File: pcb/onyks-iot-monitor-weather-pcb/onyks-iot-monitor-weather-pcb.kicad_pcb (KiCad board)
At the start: 2 copper layers, 100 x 100 mm, 25 parts, among them J1 53398-0371, J10 Conn_01x02_Pin, J2 53398-0371, J3 53048-0810, J4 53398-0371, J5 53398-0371, J6 53398-0371, J7 53398-0371, J8 53398-0371, J9 53398-0371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

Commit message: Updated schematic, changed and added couple of elements: 1.Changed buttons; 2.Changed Voltage Regulator; 3.Changed LED; 4.Added JTAG interface; 5.Added UART for programming; 6.Added other elements like capacitors etc.
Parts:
- S1: value BOOT -> PTS636_SK25F_SMTR_LFS; footprint 1bmoje:18259106 -> 1bmoje:PTS636SK25FSMTRLFS
- S2: value ENABLE -> PTS636_SK25F_SMTR_LFS; footprint 1bmoje:18259106 -> 1bmoje:PTS636SK25FSMTRLFS
- moved S2 33.9 mm to (199.2, 94.5)
- moved S1 20.0 mm to (199.2, 89.7)

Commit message: Done my version of PCB
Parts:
- removed U2: AMS1117, Package_TO_SOT_SMD:SOT-223-3_TabPin2
- added C6: 22uF, Capacitor_SMD:C_0201_0603Metric, F.Cu at (94.7, 54.8)
- added C7: 22uF, Capacitor_SMD:C_0201_0603Metric, F.Cu at (91.9, 54.8)
- added C8: 22uF, Capacitor_SMD:C_0201_0603Metric, F.Cu at (133.9, 78.5)
- added D1: WS2812B, LED_SMD:LED_WS2812B_PLCC4_5.0x5.0mm_P3.2mm, F.Cu at (154.1, 51.6)
- added J11: Conn_01x06_Pin, Connector_PinHeader_2.54mm:PinHeader_1x06_P2.54mm_Vertical, F.Cu at (169.0, 69.0)
- added J12: Conn_02x05_Odd_Even, Connector_PinHeader_2.54mm:PinHeader_2x05_P2.54mm_Vertical, F.Cu at (119.5, 86.5)
- added J13: Conn_01x02_Pin, Connector_PinHeader_2.54mm:PinHeader_1x02_P2.54mm_Vertical, F.Cu at (87.2, 57.8)
- added U3: TLV75733PDBV, Package_TO_SOT_SMD:SOT-23-5, F.Cu at (93.9, 60.3)
- J10: footprint Connector_Molex:Molex_SL_171971-0002_1x02_P2.54mm_Vertical -> Connector_PinHeader_2.54mm:PinHeader_1x02_P2.54mm_Vertical
- moved C4 51.8 mm to (164.5, 73.6), turned to 90 degrees
- moved J3 40.4 mm to (144.8, 83.5), turned to 180 degrees
- moved J1 40.2 mm to (101.7, 66.4)
- moved C5 39.0 mm to (173.7, 88.0), turned to 0 degrees
- moved J9 36.0 mm to (156.7, 72.9)
- moved J10 34.4 mm to (87.0, 69.0), turned to 0 degrees
- moved J7 32.3 mm to (101.7, 60.9)
- moved J2 31.6 mm to (101.7, 55.4)
- moved J6 31.4 mm to (101.7, 86.4)
- moved J4 31.4 mm to (101.7, 73.4)
- moved J5 31.4 mm to (101.7, 79.9)
- moved C2 30.3 mm to (118.0, 50.1), turned to 90 degrees
- moved S1 29.7 mm to (172.7, 76.2)
- moved S2 28.9 mm to (172.7, 83.0)
- moved Q1 28.2 mm to (88.4, 75.7)
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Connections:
- U1 pad 13: /Hall 6 -> /MTMS
- U1 pad 14: /DHT22 -> /MTDI
- U1 pad 16: /SEN0219 -> /MTCK
- U1 pad 23: /PMS_SELECT -> /MTDO
- U1 pad 26: unconnected-(U1-IO4-Pad26) -> /DHT22
- U1 pad 27: unconnected-(U1-IO16-Pad27) -> /UART_PROGRAM_RXD
- U1 pad 28: unconnected-(U1-IO17-Pad28) -> /UART_PROGRAM_TXD
- U1 pad 29: unconnected-(U1-IO5-Pad29) -> /SEN0219
- U1 pad 30: unconnected-(U1-IO18-Pad30) -> /UART_PROGRAM_DTR
- U1 pad 31: unconnected-(U1-IO19-Pad31) -> /UART_PROGRAM_RTS
- U1 pad 33: unconnected-(U1-IO21-Pad33) -> /PMS_SELECT
- U1 pad 37: unconnected-(U1-IO23-Pad37) -> /LED
- U1 pad 9: unconnected-(U1-IO33-Pad9) -> /Hall 6
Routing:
- net GND: track 256.8 -> 100.2 mm, vias 7 -> 17
- net /3V3: track 118.6 -> 213.6 mm, vias 6 -> 8
- net /EN: track 103.2 -> 190.7 mm, vias 2 -> 5
- net VCC: track 138.5 -> 223.2 mm, vias 9 -> 11
- net /MTMS: track 0.00 -> 33.2 mm
- net /IO0: track 137.0 -> 104.7 mm, vias 0 -> 4
- net /DHT22: track 50.8 -> 20.8 mm
- net /UART_PROGRAM_DTR: track 0.00 -> 28.4 mm
- net /UART_PROGRAM_RTS: track 0.00 -> 27.9 mm
- net /MTDO: track 0.00 -> 27.3 mm, vias 0 -> 5
- net /UART_PROGRAM_RXD: track 0.00 -> 27.3 mm, vias 0 -> 1
- net /UART_PROGRAM_TXD: track 0.00 -> 27.2 mm, vias 0 -> 1
- net /MTDI: track 0.00 -> 23.6 mm
- net /MTCK: track 0.00 -> 22.0 mm, vias 0 -> 2
- net /PMS_PWM: track 40.8 -> 58.4 mm, vias 1 -> 5
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- added copper zone on B.Cu, net GND
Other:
- board size 100 x 100 mm -> 100 x 55.8 mm

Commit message: Few corrections, small ammount of parts were not connected to the ground.
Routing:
- net GND: track 100.2 -> 118.6 mm, vias 17 -> 20
- net /3V3: track 213.6 -> 226.6 mm, vias 8 -> 10
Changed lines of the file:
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@@
+	)
+	(segment
+		(start 96.25 54.5)
+		(end 96 54.75)
+		(width 0.4)
+		(layer "F.Cu")
+		(net 1)
 	)
 	(segment
@@
 	)
 	(segment
+		(start 173.36 88)
+		(end 171.75 88)
+		(width 0.4)
+		(layer "F.Cu")
+		(net 1)
+	)
+	(segment
+		(start 131.75 72.7)
+		(end 131.75 71)
+		(width 0.6)
+		(layer "F.Cu")
+		(net 1)
+	)
+	(segment
 		(start 149.5 50)
 		(end 147.5 50)
@@
 	)
 	(segment
+		(start 92.225 54.75)
+		(end 92.225 53.025)
+		(width 0.4)
+		(layer "F.Cu")
+		(net 1)
+	)
+	(segment
+		(start 131.8 78.5)
+		(end 132.5 78.5)
+		(width 0.6)
+		(layer "F.Cu")
+		(net 1)
+	)
+	(segment
 		(start 118 48.86)
 		(end 118 49.685)
@@
 	)
 	(segment
+		(start 133.675 75.325)
+		(end 132.5 76.5)
+		(width 0.4)
+		(layer "F.Cu")
+		(net 1)
+	)
+	(segment
 		(start 101.7 53.55)
 		(end 101.7 55.25)
@@
 	)
 	(segment
+		(start 133.675 74.3)
+		(end 133.675 75.325)
+		(width 0.4)
+		(layer "F.Cu")
+		(net 1)
+	)
+	(segment
+		(start 96.25 53)
+		(end 96.25 54.5)
+		(width 0.4)
+		(layer "F.Cu")
+		(net 1)
+	)
+	(segment
 		(start 122.25 89)
 		(end 122 88.75)
@@
 	)
 	(segment
-		(start 131.8 78.5)
-		(end 133.61 78.5)
-		(width 0.6)
+		(start 92.225 53.025)
+		(end 92.25 53)
+		(width 0.2)
+		(layer "F.Cu")
+		(net 1)
+	)
+	(segment
+		(start 96 54.75)
+		(end 95.05 54.75)
+		(width 0.4)
+		(layer "F.Cu")
+		(net 1)
+	)
+	(segment
+		(start 132.5 76.5)
+		(end 132.5 78.5)
+		(width 0.4)
 		(layer "F.Cu")
 		(net 1)
@@
 	)
 	(segment
+		(start 132.5 78.5)
+		(end 133.61 78.5)
+		(width 0.6)
+		(layer "F.Cu")
+		(net 1)
+	)
+	(segment
+		(start 131.5 70.75)
+		(end 127.75 70.75)
+		(width 0.6)
+		(layer "F.Cu")
+		(net 1)
+	)
+	(segment
+		(start 131.75 71)
+		(end 131.5 70.75)
+		(width 0.6)
+		(layer "F.Cu")
+		(net 1)
+	)
+	(segment
 		(start 115.15 48.85)
 		(end 115.16 48.86)
@@
 	)
 	(via
+		(at 92.25 53)
+		(size 1.2)
+		(drill 0.6)
+		(layers "F.Cu" "B.Cu")
+		(free yes)
+		(net 1)
+	)
+	(via
 		(at 101.7 59.2)
 		(size 1.2)
@@
 	)
 	(via
+		(at 171.75 88)
+		(size 1.2)
+		(drill 0.6)
+		(layers "F.Cu" "B.Cu")
+		(net 1)
+	)
+	(via
 		(at 160.25 72.75)
 		(size 1.2)
@@
 	)
 	(via
+		(at 96.25 53)
+		(size 1.2)
+		(drill 0.6)
+		(layers "F.Cu" "B.Cu")
+		(free yes)
+		(net 1)
+	)
+	(via
 		(at 122.75 54.25)
 		(size 1.2)
@@
 		(drill 0.6)
 		(layers "F.Cu" "B.Cu")
+		(net 1)
+	)
+	(segment
+		(start 146 83.5)
+		(end 146 81.75)
+		(width 0.6)
+		(layer "B.Cu")
 		(net 1)
 	)
@@
 	)
 	(segment
+		(start 132.45 74.3)
+		(end 133.025 74.3)
+		(width 0.4)
+		(layer "F.Cu")
+		(net 35)
+	)
+	(segment
 		(start 119.46 89.46)
 		(end 120 90)
 		(width 0.6)
+		(layer "F.Cu")
+		(net 35)
+	)
+	(segment
+		(start 131.75 75)
+		(end 132.45 74.3)
+		(width 0.4)
 		(layer "F.Cu")
 		(net 35)
@@
 	)
 	(segment
+		(start 133.7 71.2)
+		(end 133.7 72.7)
+		(width 0.4)
+		(layer "F.Cu")
+		(net 35)
+	)
+	(segment
 		(start 136.75 78.5)
 		(end 134.41 78.5)
@@
 		(net 35)
 	)
+	(segment
+		(start 131.25 75)
+		(end 131.75 75)
+		(width 0.4)
+		(layer "F.Cu")
+		(net 35)
+	)
 	(via
 		(at 95 57.25)
@@
 		(size 1.2)
 		(drill 0.6)
+		(layers "F.Cu" "B.Cu")
+		(net 35)
+	)
+	(via
+		(at 131.25 75)
+		(size 0.6)
+		(drill 0.3)
+		(layers "F.Cu" "B.Cu")
+		(net 35)
+	)
+	(via
+		(at 133.7 71.2)
+		(size 0.6)
+		(drill 0.3)
 		(layers "F.Cu" "B.Cu")
 		(net 35)
@@
 	)
 	(segment
+		(start 131.25 75)
+		(end 131.25 74)
+		(width 0.4)
+		(layer "B.Cu")
+		(net 35)
+	)
+	(segment
+		(start 131.5 73.75)
+		(end 134.325 73.75)
+		(width 0.4)
+		(layer "B.Cu")
+		(net 35)
+	)
+	(segment
 		(start 99.75 49.75)
 		(end 101.5 49.75)
@@
 		(end 116.75 51.75)
 		(width 0.6)
+		(layer "B.Cu")
+		(net 35)
+	)
+	(segment
+		(start 134.325 73.75)
+		(end 134.325 76.25)
+		(width 0.4)
 		(layer "B.Cu")
 		(net 35)
@@
 	)
 	(segment
+		(start 133.7 71.95)
+		(end 134.325 72.575)
+		(width 0.4)
+		(layer "B.Cu")
+		(net 35)
+	)
+	(segment
+		(start 133.7 71.2)
+		(end 133.7 71.95)
+		(width 0.4)
+		(layer "B.Cu")
+		(net 35)
+	)
+	(segment
 		(start 95 91.5)
 		(end 96 92.5)
@@
 	)
 	(segment
+		(start 131.25 74)
+		(end 131.5 73.75)
+		(width 0.4)
+		(layer "B.Cu")
+		(net 35)
+	)
+	(segment
 		(start 136.75 77.5)
 		(end 136.75 78.5)
@@
 		(layer "B.Cu")
 		(net 35)
+	)
+	(segment
+		(start 134.325 72.575)
+		(end 134.325 73.75)
+		(width 0.4)
+		(layer "B.Cu")
+		(net 35)

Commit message: Changed ground planes, and overall small changes
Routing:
- net /3V3: track 226.6 -> 230.1 mm
- net /PMS_PWM: track 58.4 -> 58.1 mm, vias 5 -> 4
- net GND: vias 20 -> 19

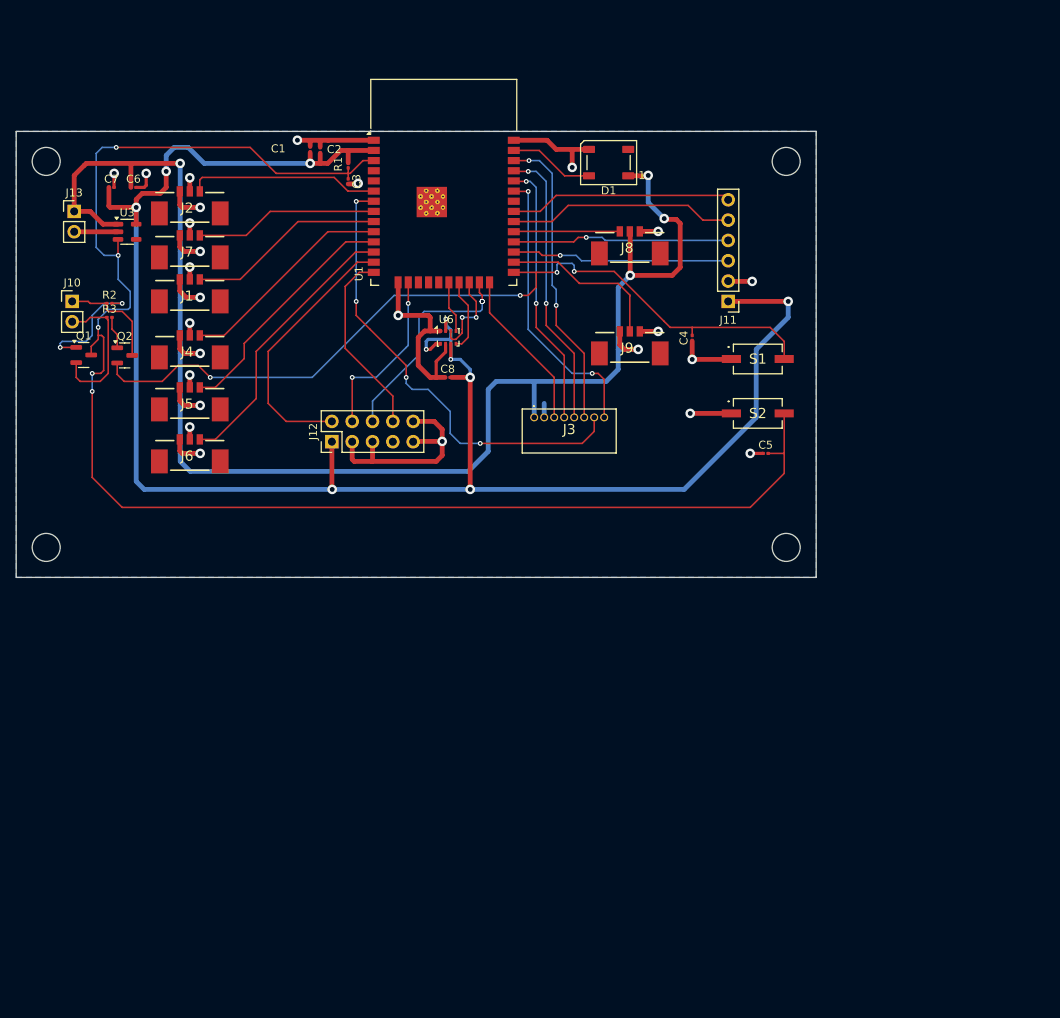
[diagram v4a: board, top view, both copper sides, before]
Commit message: CheckedJLCPCBDesignRules, the only remaining errors are due to holes in esp 32 module
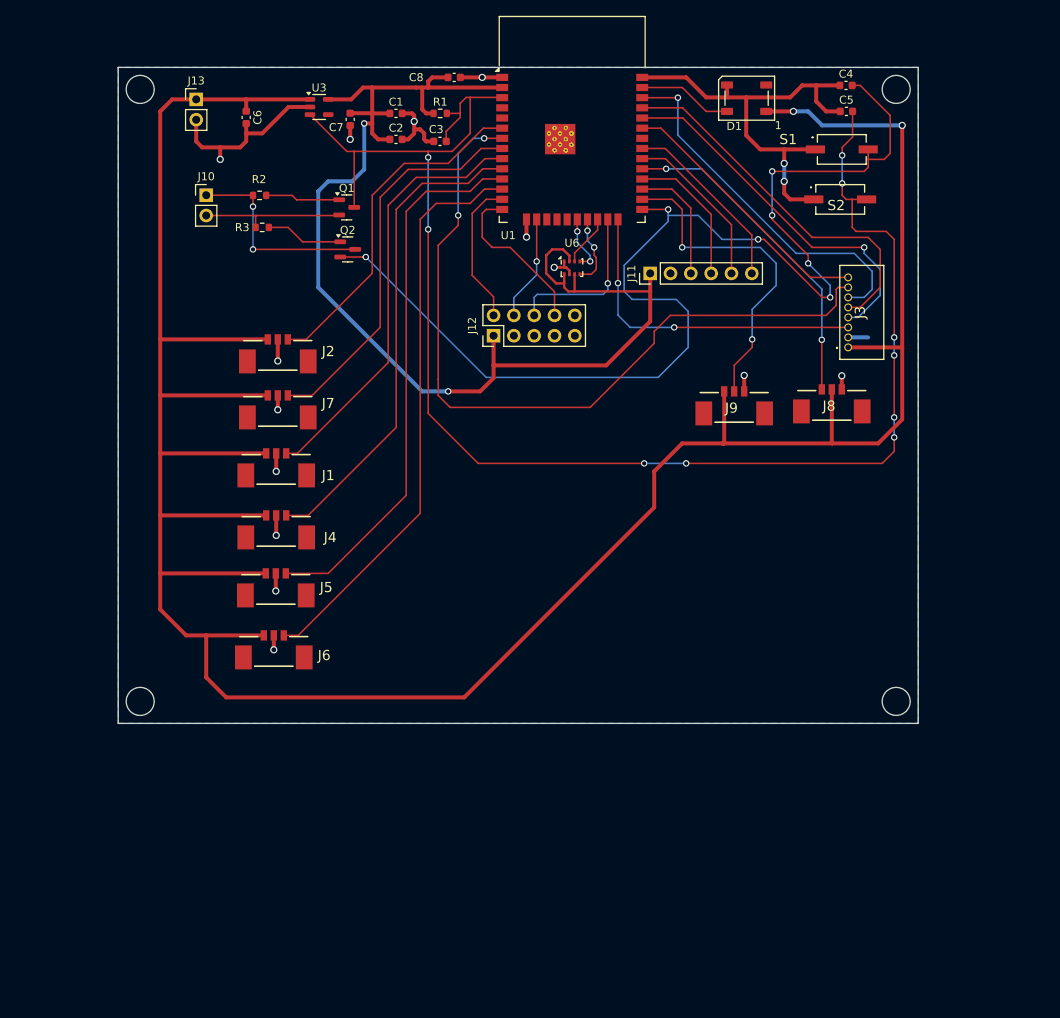
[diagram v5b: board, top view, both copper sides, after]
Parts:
- C1, C2, C3, C4, C5, C6, C7, C8: footprint Capacitor_SMD:C_0201_0603Metric -> Capacitor_SMD:C_0603_1608Metric
- R1, R2, R3: footprint Resistor_SMD:R_0201_0603Metric -> Resistor_SMD:R_0603_1608Metric
- moved C5 43.9 mm to (183.8, 45.2)
- moved J3 40.2 mm to (184.0, 74.8), turned to -90 degrees
- moved Q1 37.7 mm to (121.3, 57.2)
- moved C8 37.5 mm to (134.8, 41.0), turned to 180 degrees
- moved C4 37.0 mm to (183.7, 42.0), turned to 0 degrees
- moved J8 32.1 mm to (181.9, 80.2)
- moved C7 31.0 mm to (121.8, 46.2), turned to -90 degrees
- moved Q2 30.9 mm to (121.4, 62.5)
- moved S2 28.7 mm to (183.0, 56.2)
- moved U3 28.6 mm to (117.9, 44.7)
- moved S1 28.2 mm to (183.2, 50.0)
- moved J6 26.7 mm to (112.2, 110.9)
- moved J5 25.6 mm to (112.5, 103.2)
- moved J4 25.0 mm to (112.5, 95.9)
- moved J1 24.3 mm to (112.5, 88.2)
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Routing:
- net VCC: track 223.2 -> 349.0 mm, vias 11 -> 2
- net /3V3: track 230.1 -> 154.2 mm, vias 10 -> 2
- net /IO0: track 104.7 -> 152.4 mm, vias 4 -> 7
- net /PMS_PWM: track 58.1 -> 97.7 mm, vias 4 -> 2
- net /Hall 2: track 30.4 -> 68.3 mm
- net /Hall 3: track 34.9 -> 71.9 mm
- net /Hall 1: track 27.1 -> 60.9 mm
- net /Hall 6: track 24.7 -> 53.8 mm
- net /SEN0219: track 13.3 -> 41.2 mm, vias 0 -> 2
- net /Hall 4: track 23.0 -> 49.1 mm
- net /PMS_SET: track 20.2 -> 41.4 mm, vias 0 -> 2
- net /DHT22: track 20.8 -> 41.0 mm, vias 0 -> 2
- net /Hall 5: track 24.0 -> 43.4 mm
- net /MTMS: track 33.2 -> 18.3 mm
- net /PMS_RXD: track 33.3 -> 46.4 mm, vias 2 -> 1
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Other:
- board size 100 x 55.8 mm -> 100 x 82 mm

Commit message: Mistake Correction
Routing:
- net /IO0: track 152.4 -> 153.6 mm
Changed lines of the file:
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@@
 	)
 	(segment
-		(start 161.5 58.75)
-		(end 161.5 59)
+		(start 164 74.75)
+		(end 160.25 78.5)
+		(width 0.2)
+		(layer "B.Cu")
+		(net 36)
+	)
+	(segment
+		(start 162.5 68.75)
+		(end 164 70.25)
+		(width 0.2)
+		(layer "B.Cu")
+		(net 36)
+	)
+	(segment
+		(start 160.25 78.5)
+		(end 138.75 78.5)
 		(width 0.2)
 		(layer "B.Cu")
@@
 	)
 	(segment
-		(start 138.75 78.5)
-		(end 123.7 63.45)
+		(start 156 67.75)
+		(end 157 68.75)
 		(width 0.2)
 		(layer "B.Cu")
@@
 	)
 	(segment
-		(start 164 74.75)
-		(end 160.25 78.5)
+		(start 161.5 59)
+		(end 156 64.5)
+		(width 0.2)
+		(layer "B.Cu")
+		(net 36)
+	)
+	(segment
+		(start 179 64.25)
+		(end 181.75 67)
+		(width 0.2)
+		(layer "B.Cu")
+		(net 36)
+	)
+	(segment
+		(start 126.75 64.5)
+		(end 125.7 63.45)
+		(width 0.2)
+		(layer "B.Cu")
+		(net 36)
+	)
+	(segment
+		(start 181.75 67)
+		(end 181.75 68.5)
+		(width 0.2)
+		(layer "B.Cu")
+		(net 36)
+	)
+	(segment
+		(start 161.5 57.505)
+		(end 161.5 59)
+		(width 0.2)
+		(layer "B.Cu")
+		(net 36)
+	)
+	(segment
+		(start 138.75 78.5)
+		(end 126.75 66.5)
 		(width 0.2)
 		(layer "B.Cu")
@@
 	)
 	(segment
-		(start 161.5 57.505)
-		(end 161.5 58.75)
-		(width 0.2)
-		(layer "B.Cu")
-		(net 36)
-	)
-	(segment
-		(start 179 64.25)
-		(end 181.75 67)
-		(width 0.2)
-		(layer "B.Cu")
-		(net 36)
-	)
-	(segment
-		(start 156 64.5)
-		(end 156 67.75)
-		(width 0.2)
-		(layer "B.Cu")
-		(net 36)
-	)
-	(segment
-		(start 156 67.75)
-		(end 157 68.75)
-		(width 0.2)
-		(layer "B.Cu")
-		(net 36)
-	)
-	(segment
-		(start 181.75 67)
-		(end 181.75 68.5)
-		(width 0.2)
-		(layer "B.Cu")
-		(net 36)
-	)
-	(segment
-		(start 161.5 59)
-		(end 156 64.5)
+		(start 126.75 66.5)
+		(end 126.75 64.5)
 		(width 0.2)
 		(layer "B.Cu")
@@
 	)
 	(segment
-		(start 162.5 68.75)
-		(end 164 70.25)
+		(start 172.75 61.25)
+		(end 168.25 61.25)
 		(width 0.2)
 		(layer "B.Cu")
@@
 	)
 	(segment
-		(start 172.75 61.25)
-		(end 168.25 61.25)
+		(start 125.7 63.45)
+		(end 123.7 63.45)
 		(width 0.2)
 		(layer "B.Cu")
@@
 	)
 	(segment
-		(start 160.25 78.5)
-		(end 138.75 78.5)
+		(start 156 64.5)
+		(end 156 67.75)
 		(width 0.2)
 		(layer "B.Cu")

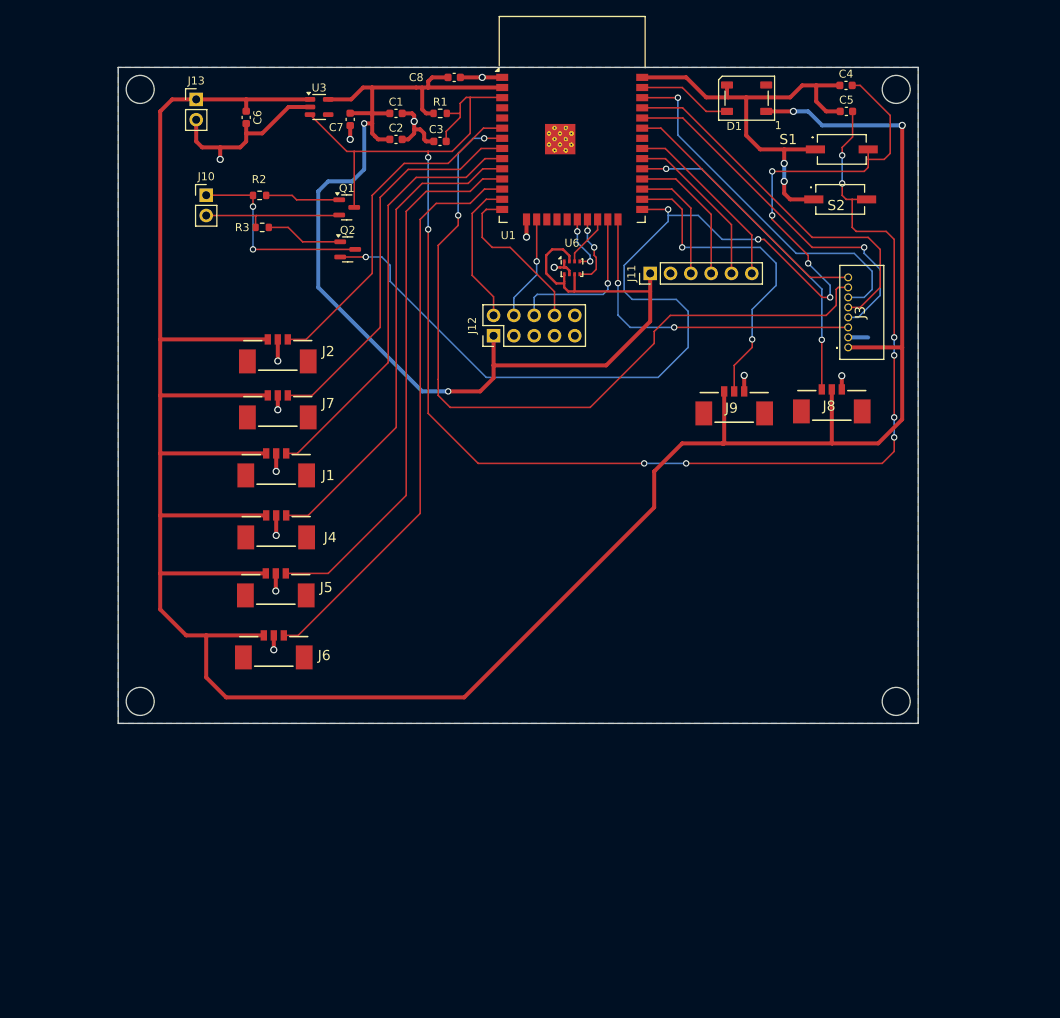
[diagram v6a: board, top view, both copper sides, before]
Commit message: U6,J3 ground pads are not connected to the ground zone automatically(due to their footprints). Ground pads C2 and C1 are connected to the ground plane via route. Overall little changes in layout. Ground pads are connected to the ground plane automatically wherever possible. Added top ground plane.
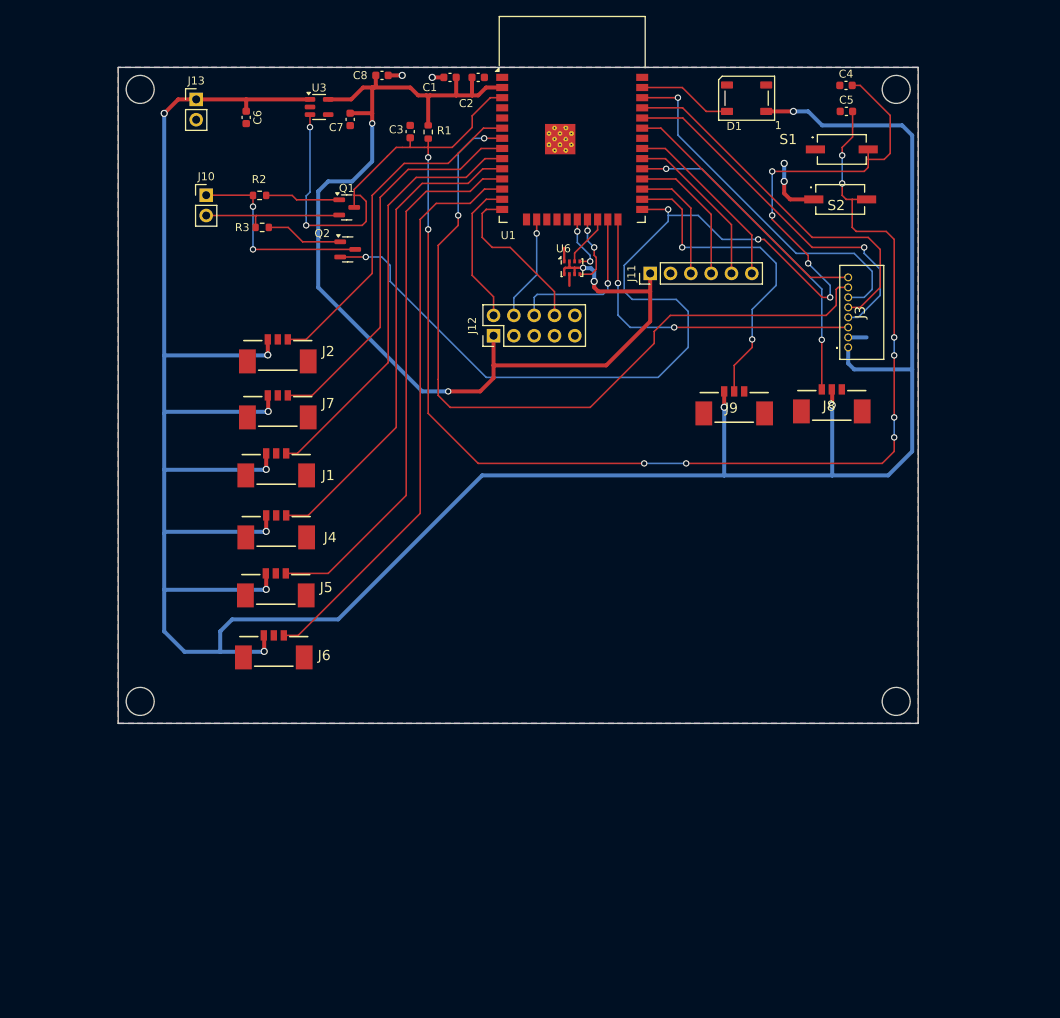
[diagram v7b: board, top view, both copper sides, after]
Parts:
- moved C2 12.9 mm to (137.8, 41.0)
- moved C8 9.03 mm to (125.7, 40.8)
- moved C1 8.11 mm to (134.2, 41.0), turned to 180 degrees
- moved C3 3.92 mm to (129.2, 47.8), turned to 90 degrees
- moved R1 2.77 mm to (131.5, 47.8), turned to -90 degrees
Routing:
- net GND: track 120.8 -> 16.4 mm, vias 16 -> 4
- net VCC: track 349.0 -> 362.9 mm, vias 2 -> 10
- net /3V3: track 154.2 -> 141.7 mm, vias 2 -> 4
- net /EN: track 191.5 -> 199.6 mm, vias 10 -> 12
- added copper zone on F.Cu, net GND
